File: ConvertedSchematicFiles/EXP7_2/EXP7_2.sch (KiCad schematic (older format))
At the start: 8 parts

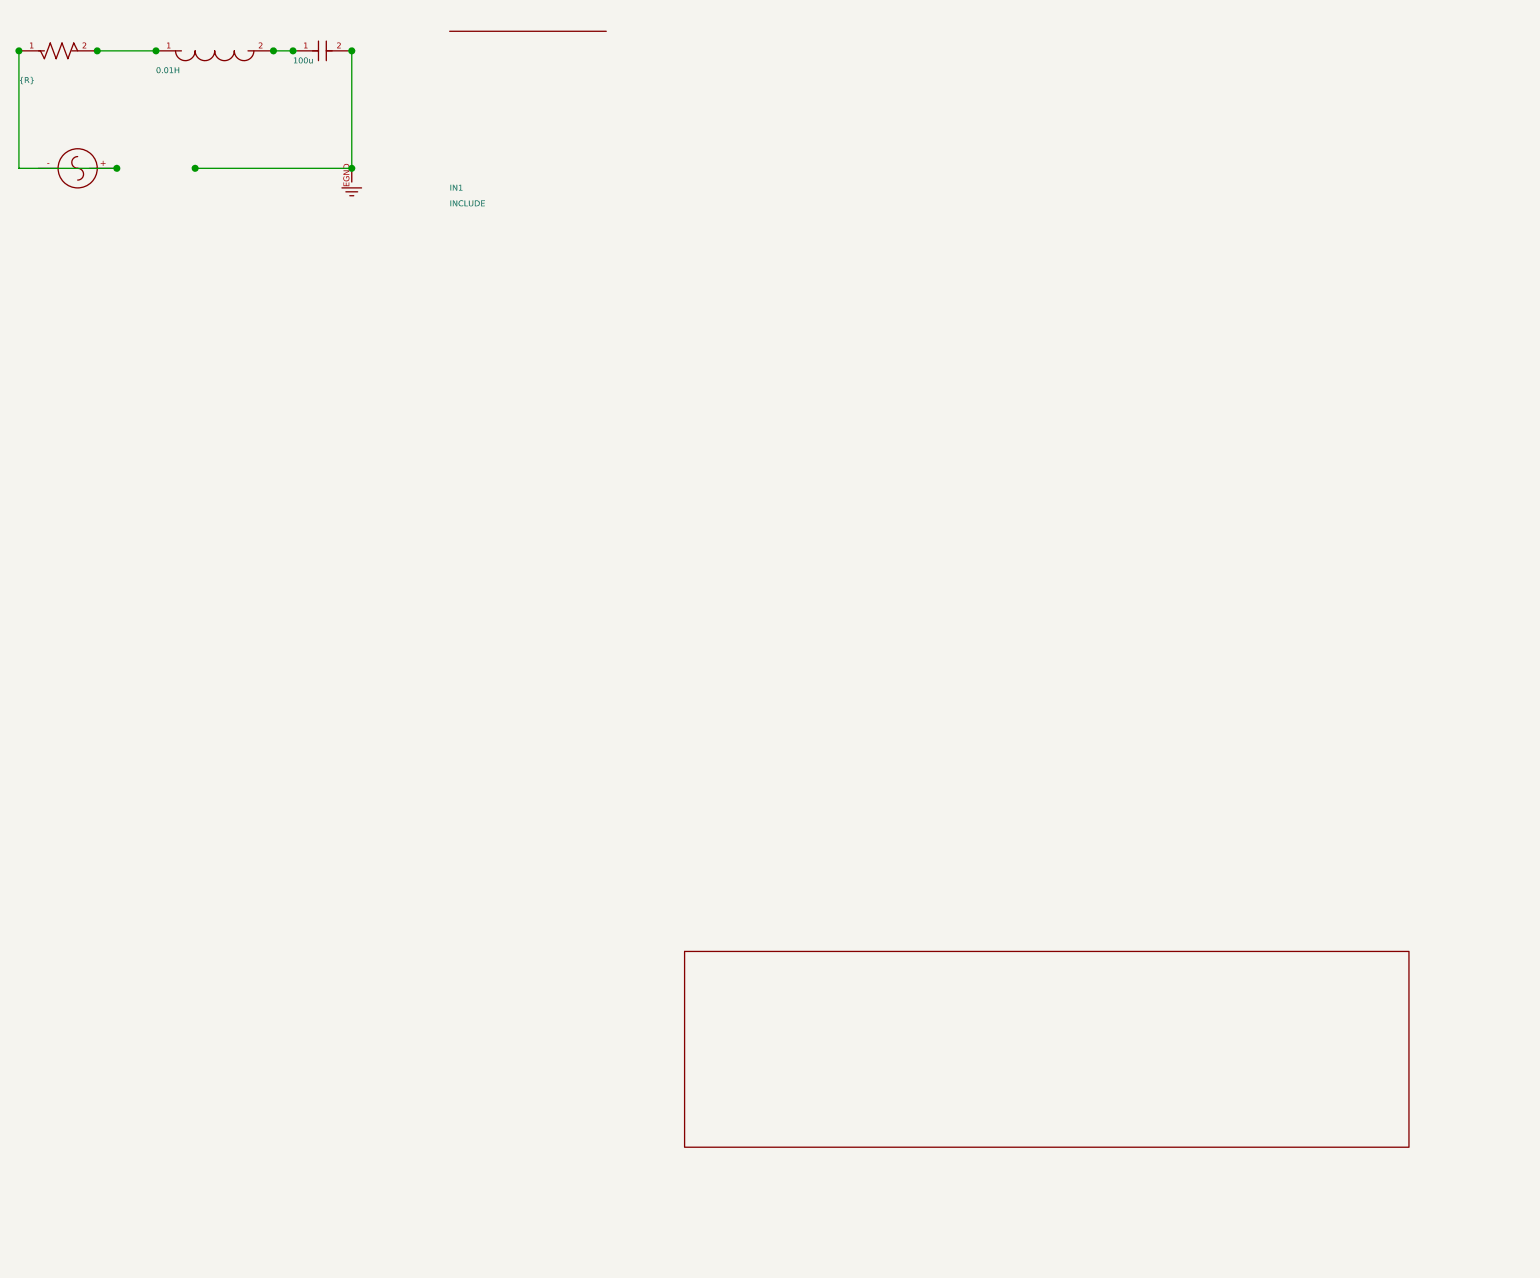
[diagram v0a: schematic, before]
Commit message: Excluded some components. These no longer appear after conversion. When calling shell commands, filenames are in "quotes"
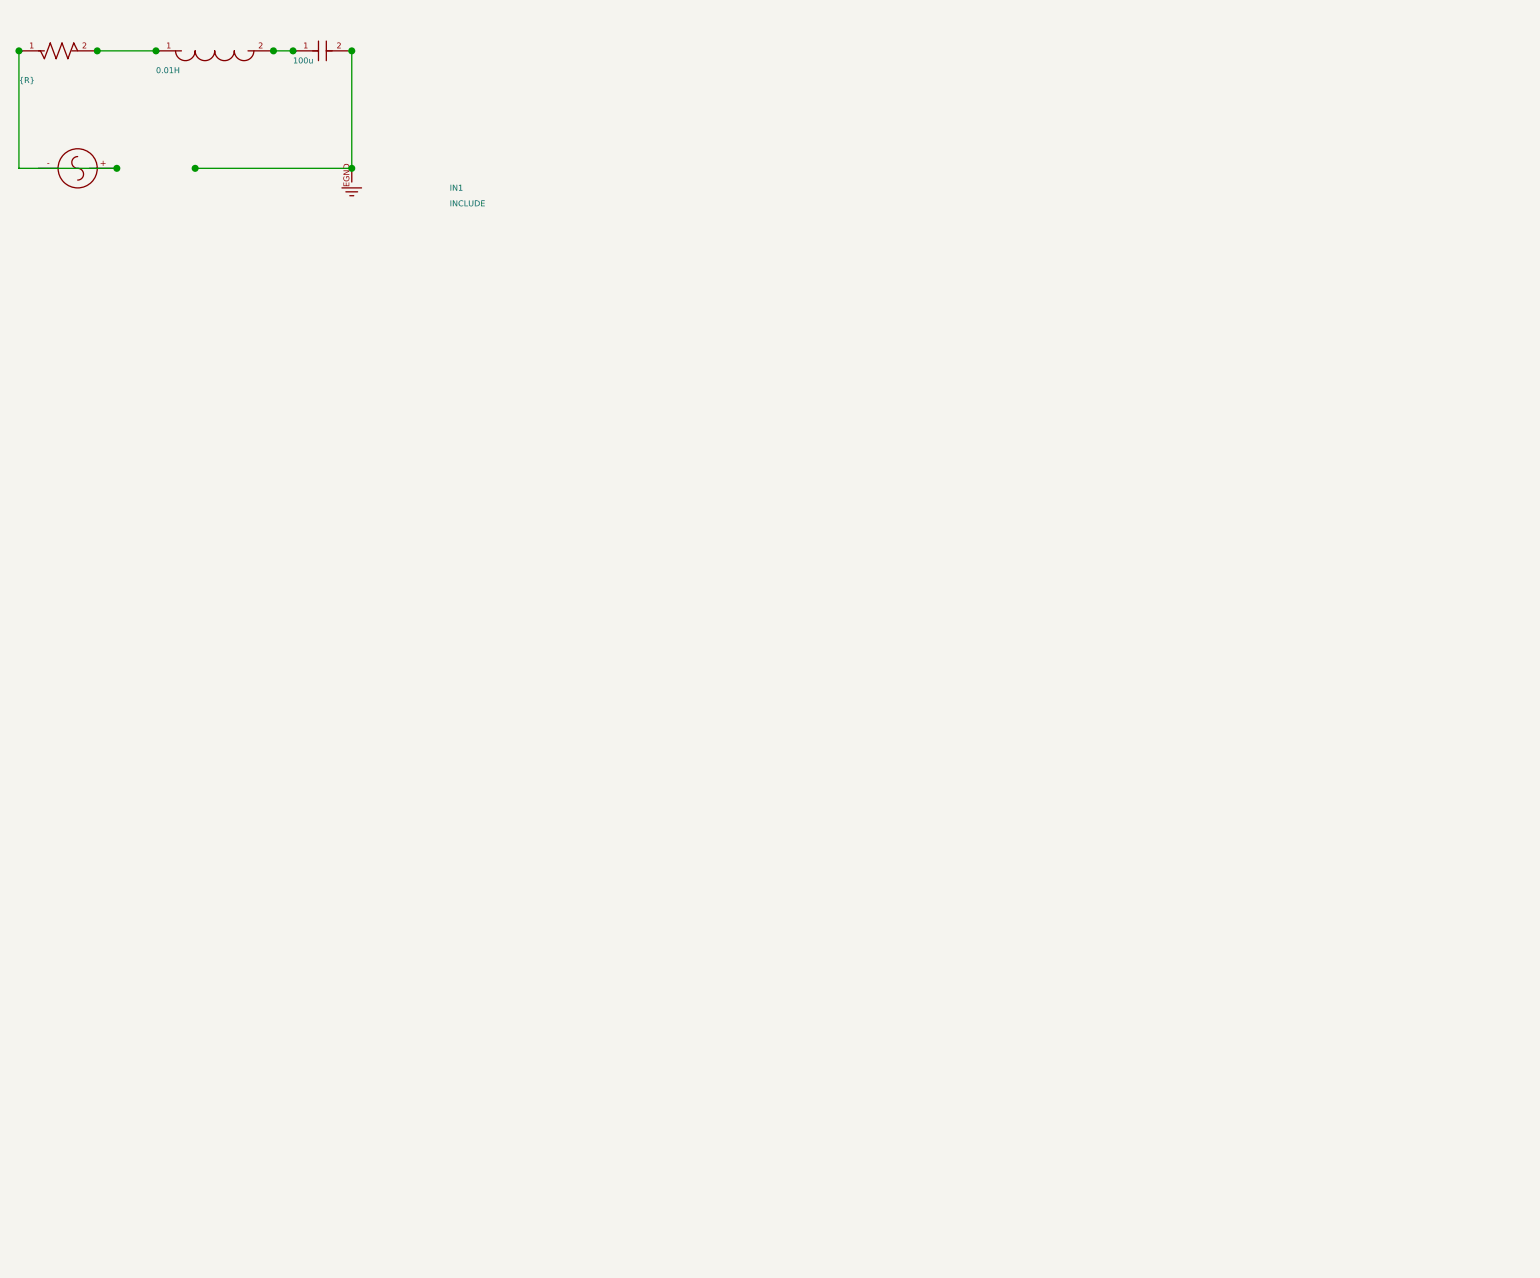
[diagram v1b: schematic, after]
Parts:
- removed PM1: PARAM, symbol PARAM_PSPICE
- removed titleblk: titleblk, symbol TITLEBLK_PSPICE
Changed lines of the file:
@@
-	1    0    0    1
-$EndComp
-$Comp
-L PARAM_PSPICE PM1
-U 1 1 99885386
-P 5200 1500
-F 0 "PM1" H 5200 1500 30  0001 L CNN
-F 1 "PARAM" H 5200 1580 30  0001 L CNN
-	1    5200 1500
-	1    0    0    1
-$EndComp
-$Comp
-L TITLEBLK_PSPICE titleblk
-U 1 1 39760492
-P 9700 7200
-F 0 "titleblk" H 19400 14400 30  0001 L CNN
-F 1 "titleblk" H 19400 14480 30  0001 L CNN
-	1    9700 7200
 	1    0    0    1
 $EndComp

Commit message: Ports issue fixed. Now annotation for ports is #PWR? function added "itos"
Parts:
- removed GND_EARTH: GND_EARTH, symbol GND_EARTH_PSPICE
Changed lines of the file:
@@
 $EndDescr
 $Comp
-L GND_EARTH_PSPICE GND_EARTH
+L GND_EARTH_PSPICE #PWR1
 U 1 1 14289383
 P 4300 2200
-F 0 "GND_EARTH" H 8600 4400 30  0001 L CNN
+F 0 "#PWR1" H 8600 4400 30  0001 L CNN
 F 1 "GND_EARTH" H 8600 4480 30  0001 L CNN
 	1    4300 2200

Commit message: Added LICENSE.txt
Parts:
- V1: value VAC -> AC
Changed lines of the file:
@@
 $EndDescr
 $Comp
-L GND_EARTH_PSPICE #PWR1
+L GND #PWR1
 U 1 1 14289383
 P 4300 2200
@@
 P 3100 2200
 F 0 "V1" H 3100 2200 30  0001 L CNN
-F 1 "VAC" H 3100 2280 30  0001 L CNN
+F 1 "AC" H 3100 2280 30  0001 L CNN
 	1    3100 2200
 	0    1    -1    0

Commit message: Orientation fix. Library components are now inverted, with +ve y axis going up. In Schematic files, +ve y axis is downwards. This is how the KiCad libraries are. As a result of the above fixed, the converted GND is now oriented correctly.
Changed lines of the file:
@@
 F 1 "GND_EARTH" H 8600 4480 30  0001 L CNN
 	1    4300 2200
-	1    0    0    1
+	1    0    0    -1
 $EndComp
 $Comp
@@
 F 1 "AC" H 3100 2280 30  0001 L CNN
 	1    3100 2200
-	0    1    -1    0
+	0    -1    -1    0
 $EndComp
 $Comp
@@
 F 1 "{R}" H 2600 1750 30  0000 L CNN
 	1    2600 1600
-	1    0    0    1
+	1    0    0    -1
 $EndComp
 $Comp
@@
 F 1 "INCLUDE" H 4800 2380 30  0000 L CNN
 	1    4800 2300
-	1    0    0    1
+	1    0    0    -1
 $EndComp
 $Comp
@@
 F 1 "100u" H 4000 1650 30  0000 L CNN
 	1    4000 1600
-	1    0    0    1
+	1    0    0    -1
 $EndComp
 $Comp
@@
 F 1 "0.01H" H 3300 1700 30  0000 L CNN
 	1    3300 1600
-	1    0    0    1
+	1    0    0    -1
 $EndComp
 Wire Wire Line

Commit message: Removed the use of exec, wrote basename function, made integration with eSim easier.
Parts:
- added PM1: PARAM, symbol PARAM_PSPICE
- added titleblk: titleblk, symbol titleblk_PSPICE
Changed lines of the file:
@@
-EESchema Schematic File Version 2  date Friday 04 June 1999 12:56:22 AM IST
+EESchema Schematic File Version 2  date
 LIBS:power
 LIBS:device
@@
 LIBS:contrib
 LIBS:valves
-LIBS:ConvertedSchematicFiles/EXP7_2-cache
 EELAYER 25  0
 EELAYER END
@@
 Sheet 1 1
 Title ""
-Date "04 Jun 1999"
+Date ""
 Rev ""
 Comp ""
@@
 	1    0    0    -1
 $EndComp
+$Comp
+L PARAM_PSPICE PM1
+U 1 1 99885386
+P 5200 1500
+F 0 "PM1" H 5200 1500 30  0001 L CNN
+F 1 "PARAM" H 5200 1580 30  0001 L CNN
+	1    5200 1500
+	1    0    0    -1
+$EndComp
+$Comp
+L titleblk_PSPICE titleblk
+U 1 1 39760492
+P 9700 7200
+F 0 "titleblk" H 19400 14400 30  0001 L CNN
+F 1 "titleblk" H 19400 14480 30  0001 L CNN
+	1    9700 7200
+	1    0    0    -1
+$EndComp
